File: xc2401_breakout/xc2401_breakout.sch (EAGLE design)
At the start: 11 parts, among them U1 XC2401

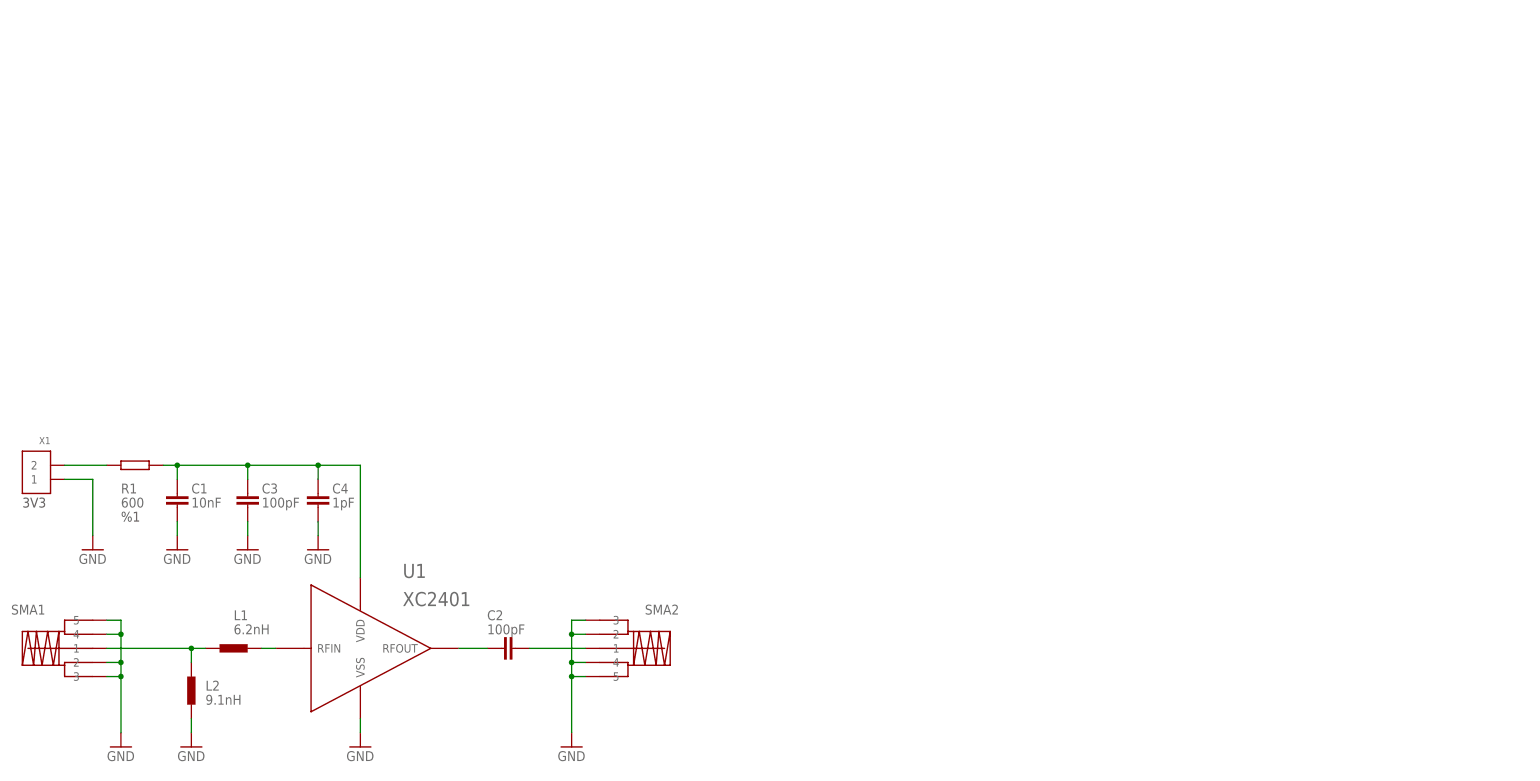
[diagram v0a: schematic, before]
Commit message: Added frame to schematic
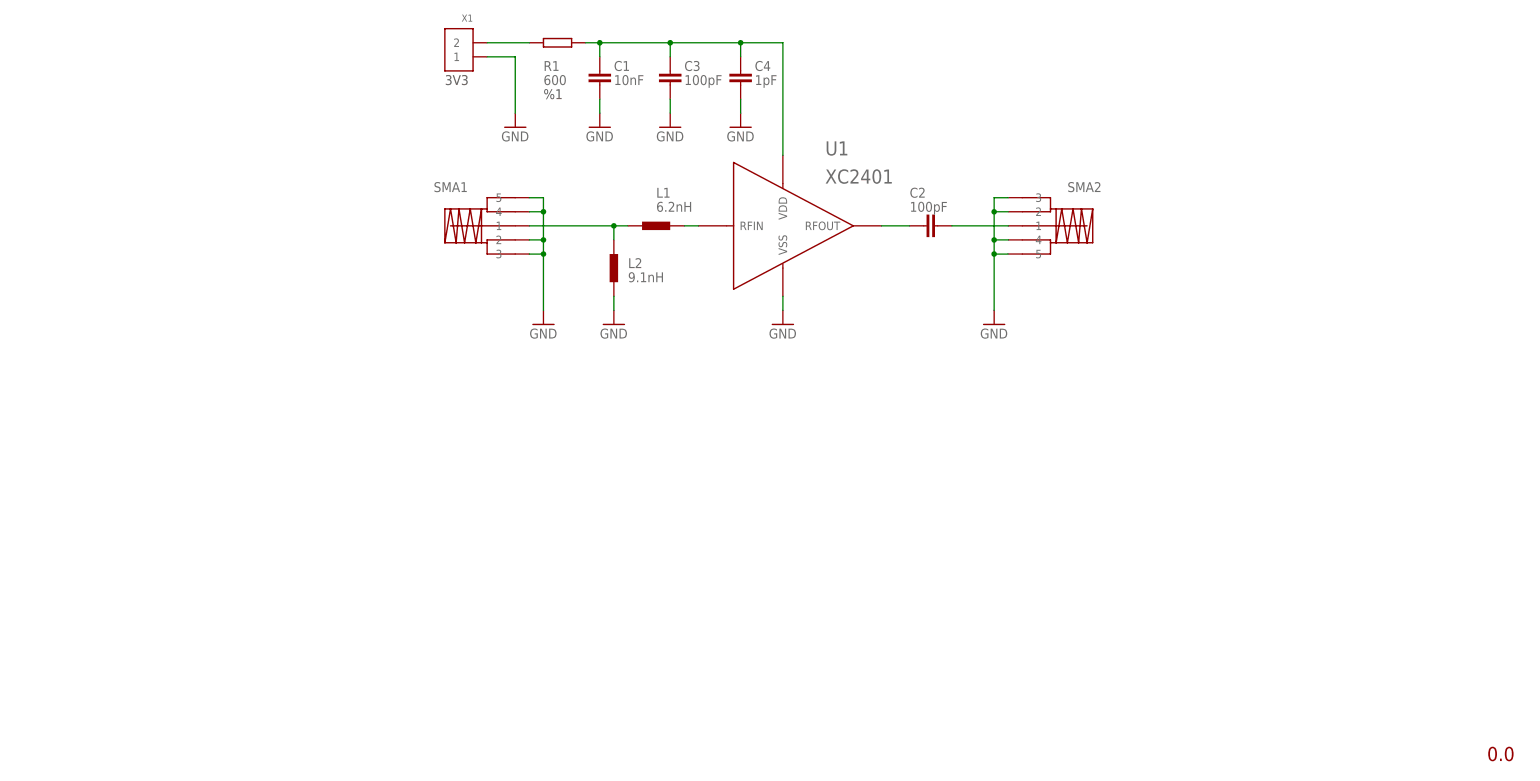
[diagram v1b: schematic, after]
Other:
- note added: "0.0"
- moved on the sheet: C1, C2, C3, C4, L1, L2, R1, SMA1, SMA2, U1, X1
